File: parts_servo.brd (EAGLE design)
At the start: 27.1 x 50 mm, 43 parts, among them Q110 PMDPB28UN, Q120 PMDPB28UN, U1 MCP1703-3302, U100 RT9625A, U20 sn65hvd72, U50 nRF51822, X60 CX3225GB16000P0HPQCC

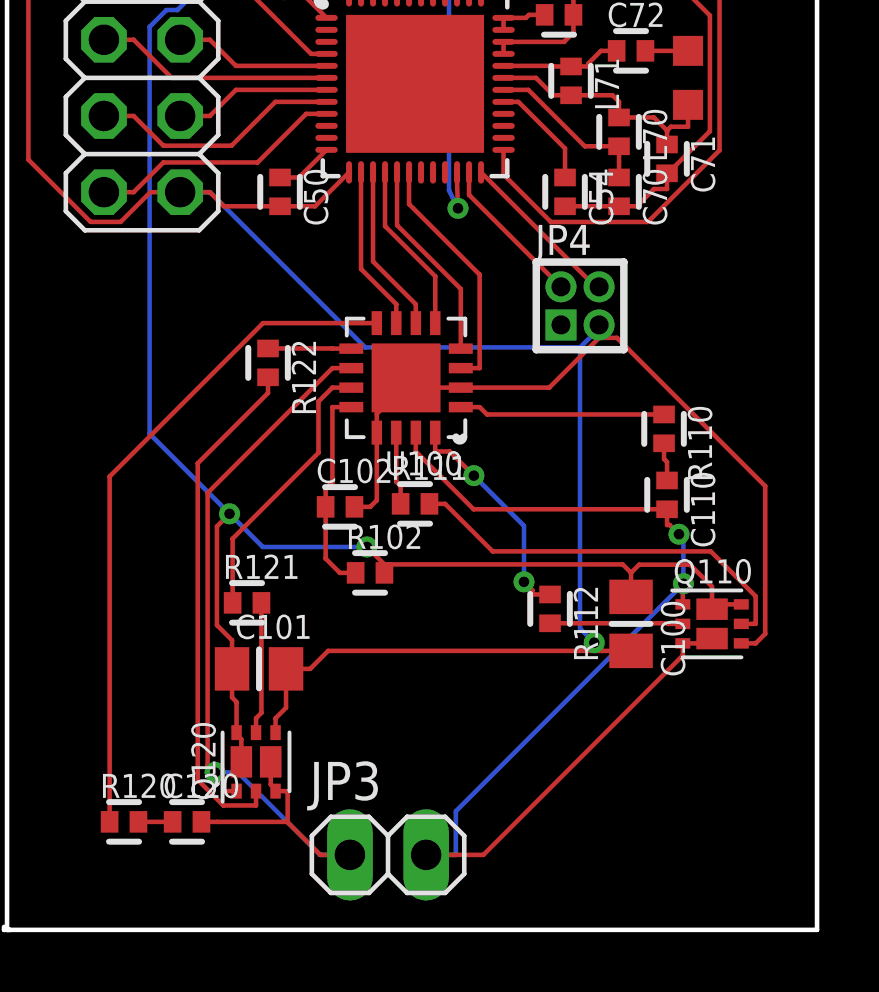
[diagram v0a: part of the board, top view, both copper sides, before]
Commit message: Fix DRC errors from via resize
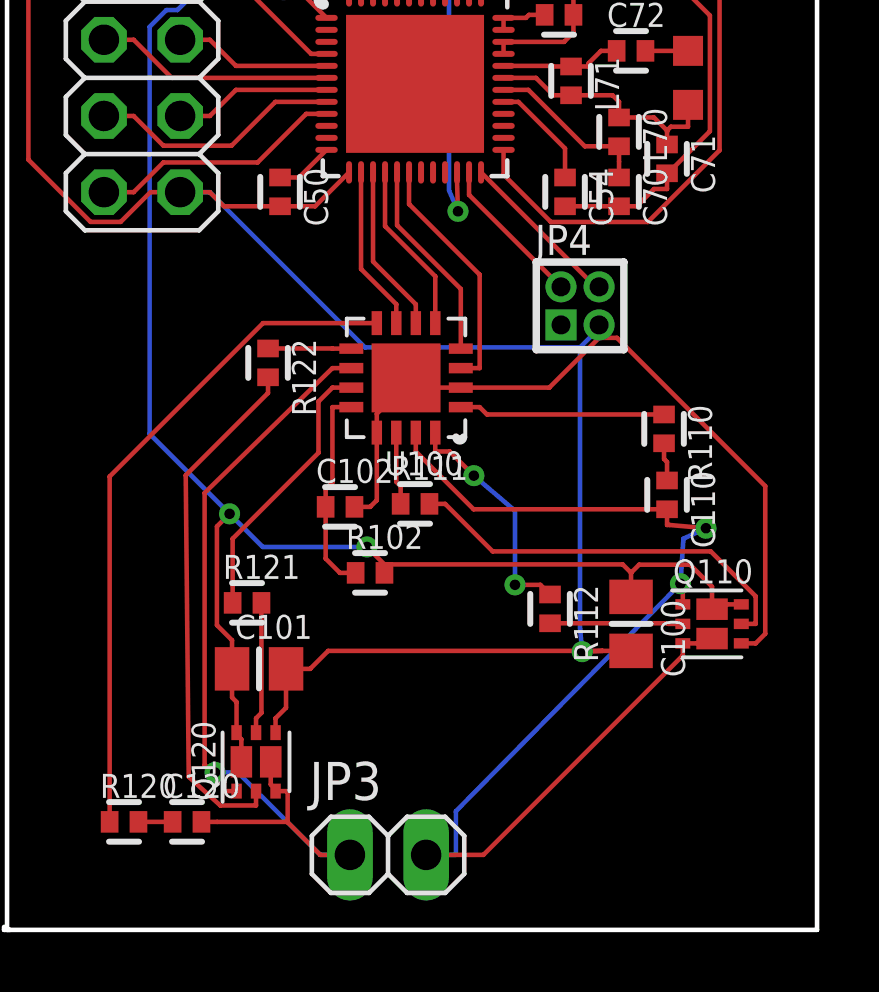
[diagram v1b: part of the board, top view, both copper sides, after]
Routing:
- net MOTOR2: track 39.2 -> 40.6 mm
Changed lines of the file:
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@@
 <contactref element="Q110" pad="4"/>
 <contactref element="Q120" pad="4"/>
-<wire x1="19.5733" y1="9.573" x2="19.8463" y2="9.3" width="0.1524" layer="1"/>
+<wire x1="19.1733" y1="9.273" x2="19.8463" y2="9.3" width="0.1524" layer="1"/>
 <wire x1="19.1" y1="19.4162" x2="19.1" y2="10.0463" width="0.1524" layer="16"/>
-<wire x1="19.1" y1="10.0463" x2="19.5733" y2="9.573" width="0.1524" layer="16"/>
+<wire x1="19.1" y1="10.0463" x2="19.1733" y2="9.273" width="0.1524" layer="16"/>
 <wire x1="19.735" y1="19.7344" x2="20.3311" y2="19.7344" width="0.1524" layer="1"/>
 <wire x1="20.3311" y1="19.7344" x2="25.2733" y2="14.7922" width="0.1524" layer="1"/>
@@
 <wire x1="6.7607" y1="24.59" x2="11.9345" y2="19.4162" width="0.1524" layer="16"/>
 <wire x1="11.9345" y1="19.4162" x2="19.1" y2="19.4162" width="0.1524" layer="16"/>
-<via x="19.5733" y="9.573" extent="1-16" drill="0.35" diameter="0.6858"/>
+<via x="19.1733" y="9.273" extent="1-16" drill="0.35" diameter="0.6858"/>
 <wire x1="19.8463" y1="9.3" x2="10.7037" y2="9.3" width="0.1524" layer="1"/>
 <wire x1="10.7037" y1="9.3" x2="10.1037" y2="8.7" width="0.1524" layer="1"/>
@@
 <contactref element="Q120" pad="P8"/>
 <contactref element="Q120" pad="1"/>
-<wire x1="10.8463" y1="18.725" x2="6.6856" y2="14.5643" width="0.1524" layer="1"/>
-<wire x1="6.6856" y1="14.5643" x2="6.6856" y2="5.4965" width="0.1524" layer="1"/>
-<wire x1="6.6856" y1="5.4965" x2="6.9337" y2="5.2484" width="0.1524" layer="1"/>
+<wire x1="10.8463" y1="18.725" x2="6.5856" y2="14.5643" width="0.1524" layer="1"/>
+<wire x1="6.5856" y1="14.5643" x2="6.5856" y2="5.4965" width="0.1524" layer="1"/>
+<wire x1="6.5856" y1="5.4965" x2="6.9337" y2="5.2484" width="0.1524" layer="1"/>
 <wire x1="7.2463" y1="4.625" x2="7.2463" y2="4.9358" width="0.1524" layer="1"/>
 <wire x1="7.2463" y1="4.9358" x2="6.9337" y2="5.2484" width="0.1524" layer="1"/>
@@
 <contactref element="R122" pad="2"/>
 <contactref element="Q120" pad="2"/>
-<wire x1="8.3" y1="4.1463" x2="7.2101" y2="4.1463" width="0.1524" layer="1"/>
-<wire x1="7.2101" y1="4.1463" x2="6.356" y2="5.0004" width="0.1524" layer="1"/>
-<wire x1="6.356" y1="5.0004" x2="6.356" y2="15.5523" width="0.1524" layer="1"/>
-<wire x1="6.356" y1="15.5523" x2="8.7" y2="17.8963" width="0.1524" layer="1"/>
+<wire x1="8.3" y1="4.1463" x2="7.1101" y2="4.1463" width="0.1524" layer="1"/>
+<wire x1="7.1101" y1="4.1463" x2="6.056" y2="5.1004" width="0.1524" layer="1"/>
+<wire x1="6.056" y1="5.1004" x2="5.956" y2="15.1523" width="0.1524" layer="1"/>
+<wire x1="5.956" y1="15.1523" x2="8.7" y2="17.8963" width="0.1524" layer="1"/>
 <wire x1="8.3" y1="4.625" x2="8.3" y2="4.1463" width="0.1524" layer="1"/>
 <wire x1="8.7" y1="18.42" x2="8.7" y2="17.8963" width="0.1524" layer="1"/>
@@
 <wire x1="13.97" y1="2.5" x2="15.8787" y2="2.5" width="0.1524" layer="1"/>
 <wire x1="15.8787" y1="2.5" x2="22.525" y2="9.1463" width="0.1524" layer="1"/>
-<wire x1="22.5461" y1="11.5393" x2="22.525" y2="11.5182" width="0.1524" layer="1"/>
+<wire x1="22.4461" y1="11.5393" x2="22.525" y2="11.5182" width="0.1524" layer="1"/>
 <wire x1="22.525" y1="11.5182" x2="22.525" y2="10.85" width="0.1524" layer="1"/>
 <wire x1="22" y1="14.02" x2="22" y2="13.4963" width="0.1524" layer="1"/>
 <wire x1="22" y1="13.4963" x2="22.0895" y2="13.4963" width="0.1524" layer="1"/>
-<wire x1="22.0895" y1="13.4963" x2="22.3977" y2="13.1881" width="0.1524" layer="1"/>
-<wire x1="22.3977" y1="13.1881" x2="22.5461" y2="13.0397" width="0.1524" layer="16"/>
-<wire x1="22.5461" y1="13.0397" x2="22.5461" y2="11.5393" width="0.1524" layer="16"/>
-<via x="22.3977" y="13.1881" extent="1-16" drill="0.35" diameter="0.6858"/>
+<wire x1="22.0895" y1="13.4963" x2="23.2977" y2="13.3881" width="0.1524" layer="1"/>
+<wire x1="23.2977" y1="13.3881" x2="22.5461" y2="13.0397" width="0.1524" layer="16"/>
+<wire x1="22.5461" y1="13.0397" x2="22.4461" y2="11.5393" width="0.1524" layer="16"/>
+<via x="23.2977" y="13.3881" extent="1-16" drill="0.35" diameter="0.6858"/>
 <wire x1="13.625" y1="15.9463" x2="15.5513" y2="14.02" width="0.1524" layer="1"/>
 <wire x1="15.5513" y1="14.02" x2="22" y2="14.02" width="0.1524" layer="1"/>
 <wire x1="13.97" y1="2.5" x2="14.9607" y2="2.5" width="0.1524" layer="16"/>
 <wire x1="14.9607" y1="2.5" x2="14.9607" y2="3.9539" width="0.1524" layer="16"/>
-<wire x1="14.9607" y1="3.9539" x2="22.5461" y2="11.5393" width="0.1524" layer="16"/>
-<via x="22.5461" y="11.5393" extent="1-16" drill="0.35" diameter="0.6858"/>
+<wire x1="14.9607" y1="3.9539" x2="22.4461" y2="11.5393" width="0.1524" layer="16"/>
+<via x="22.4461" y="11.5393" extent="1-16" drill="0.35" diameter="0.6858"/>
 <wire x1="13.625" y1="16.575" x2="13.625" y2="15.9463" width="0.1524" layer="1"/>
 <wire x1="22.525" y1="9.55" x2="22.569" y2="9.55" width="0.1524" layer="1"/>
@@
 <contactref element="R112" pad="1"/>
 <contactref element="U100" pad="16"/>
-<wire x1="17.5113" y1="11.18" x2="17.5113" y2="11.3216" width="0.1524" layer="1"/>
-<wire x1="17.5113" y1="11.3216" x2="17.2315" y2="11.6014" width="0.1524" layer="1"/>
-<wire x1="15.5609" y1="15.1405" x2="17.2315" y2="13.4699" width="0.1524" layer="16"/>
-<wire x1="17.2315" y1="13.4699" x2="17.2315" y2="11.6014" width="0.1524" layer="16"/>
-<wire x1="18.1" y1="11.18" x2="17.5113" y2="11.18" width="0.1524" layer="1"/>
+<wire x1="15.5609" y1="15.1405" x2="16.9315" y2="13.9699" width="0.1524" layer="16"/>
+<wire x1="16.9315" y1="13.9699" x2="16.9315" y2="11.5014" width="0.1524" layer="16"/>
 <wire x1="14.275" y1="16.575" x2="14.275" y2="15.9463" width="0.1524" layer="1"/>
 <wire x1="15.5609" y1="15.1405" x2="14.7551" y2="15.9463" width="0.1524" layer="1"/>
 <wire x1="14.7551" y1="15.9463" x2="14.275" y2="15.9463" width="0.1524" layer="1"/>
 <via x="15.5609" y="15.1405" extent="1-16" drill="0.35" diameter="0.6858"/>
-<via x="17.2315" y="11.6014" extent="1-16" drill="0.35" diameter="0.6858"/>
+<via x="16.9315" y="11.5014" extent="1-16" drill="0.35" diameter="0.6858"/>
+<wire x1="16.9315" y1="11.5014" x2="17.7786" y2="11.5014" width="0.1524" layer="1"/>
+<wire x1="17.7786" y1="11.5014" x2="18.1" y2="11.18" width="0.1524" layer="1"/>
 </signal>
 <signal name="BOOT2">
@@
 <contactref element="U50" pad="22"/>
 <wire x1="15" y1="25.25" x2="15" y2="24.9197" width="0.1524" layer="1"/>
-<wire x1="15" y1="24.9197" x2="15.0317" y2="24.0514" width="0.1524" layer="1"/>
+<wire x1="15" y1="24.9197" x2="15.0317" y2="23.9514" width="0.1524" layer="1"/>
 <wire x1="9.1786" y1="41.3827" x2="14.7316" y2="35.8297" width="0.1524" layer="16"/>
 <wire x1="14.7316" y1="35.8297" x2="14.7316" y2="24.6514" width="0.1524" layer="16"/>
-<wire x1="14.7316" y1="24.6514" x2="15.0317" y2="24.0514" width="0.1524" layer="16"/>
+<wire x1="14.7316" y1="24.6514" x2="15.0317" y2="23.9514" width="0.1524" layer="16"/>
 <wire x1="8.22" y1="42.9" x2="8.22" y2="42.3113" width="0.1524" layer="1"/>
 <wire x1="9.1786" y1="41.3827" x2="8.25" y2="42.3113" width="0.1524" layer="1"/>
 <wire x1="8.25" y1="42.3113" x2="8.22" y2="42.3113" width="0.1524" layer="1"/>
 <via x="9.1786" y="41.3827" extent="1-16" drill="0.35" diameter="0.6858"/>
-<via x="15.0317" y="24.0514" extent="1-16" drill="0.35" diameter="0.6858"/>
+<via x="15.0317" y="23.9514" extent="1-16" drill="0.35" diameter="0.6858"/>
 </signal>
 <signal name="DIFFERENTIAL_OUTPUT">

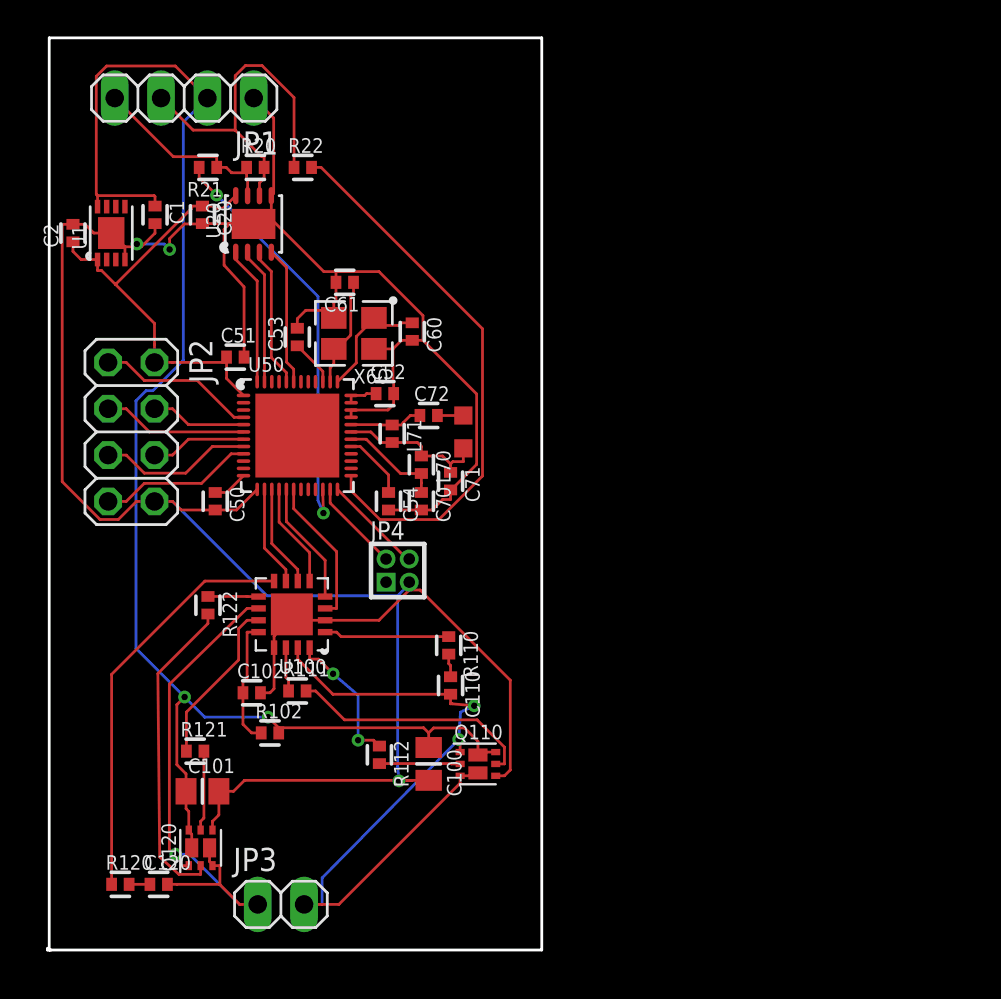
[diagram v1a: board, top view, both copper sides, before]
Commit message: Fatten some traces, fix DRC and routing
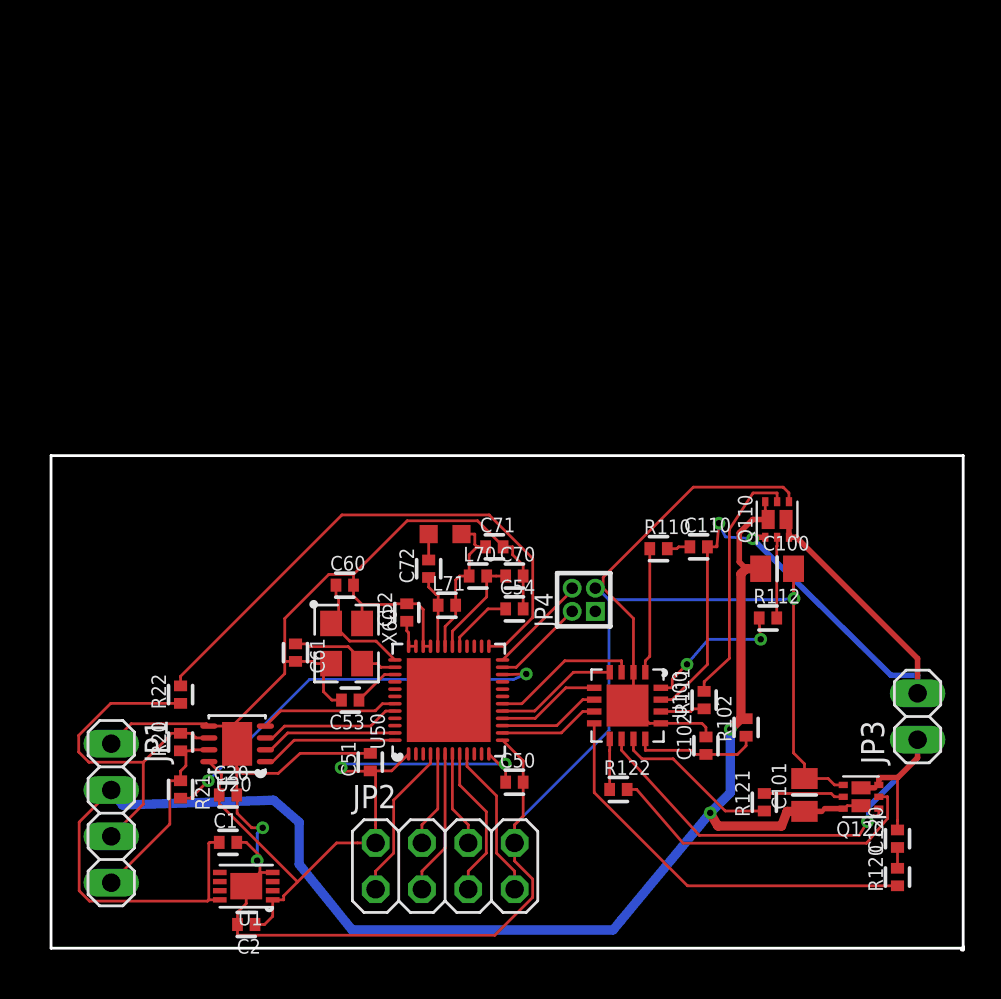
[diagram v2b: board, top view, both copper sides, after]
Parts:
- moved R120 42.6 mm to (46.5, 4.00), turned to 90 degrees
- moved C120 40.6 mm to (46.5, 6.10), turned to 90 degrees
- moved JP1 39.4 mm to (3.40, 7.50), turned to 270 degrees
- moved C2 39.1 mm to (10.8, 1.40), turned to 180 degrees
- moved U1 36.6 mm to (10.8, 3.50), turned to 180 degrees
- moved JP3 36.4 mm to (47.6, 12.8), turned to 90 degrees
- moved Q120 36.3 mm to (44.5, 8.40), turned to 180 degrees
- moved C1 34.6 mm to (9.80, 5.90), turned to 0 degrees
- moved R21 34.1 mm to (7.20, 8.80), turned to 270 degrees
- moved C101 33.0 mm to (41.4, 8.50), turned to 90 degrees
- moved C20 31.8 mm to (9.80, 8.50), turned to 0 degrees
- moved R20 31.8 mm to (7.20, 11.4), turned to 90 degrees
- moved R121 31.3 mm to (39.2, 8.10), turned to 90 degrees
- moved R22 29.7 mm to (7.20, 14.0), turned to 90 degrees
- moved JP2 29.4 mm to (21.7, 4.60), turned to 0 degrees
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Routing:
- net 3.3V: track 26.4 -> 37.6 mm, vias 0 -> 2
- net POWER_IN: track 82.6 -> 88.3 mm
- net MOTOR1: track 30.8 -> 31.3 mm
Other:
- board size 27.1 x 50 mm -> 50 x 27.1 mm

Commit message: Move programming header to edge of board
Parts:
- moved JP4 5.90 mm to (29.4, 25.1)
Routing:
- net GND: track 165.6 -> 175.8 mm
- net SWDCLK: track 5.52 -> 11.6 mm
- net SWDIO: track 5.08 -> 10.9 mm
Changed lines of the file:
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@@
 </element>
 <element name="U20" library="parts_servo" package="DFN-8(3X3)+EP" value="sn65hvd72" x="10.3" y="11.3" rot="R180"/>
-<element name="JP4" library="parts_servo" package="PINHEADER-2X2-0.05_IN" value="SWD" x="29.3" y="19.2" rot="R90"/>
+<element name="JP4" library="parts_servo" package="PINHEADER-2X2-0.05_IN" value="SWD" x="29.4" y="25.1" rot="R90"/>
 <element name="Q110" library="parts_servo" package="DFN-6(2X2)+2EP(TRANSISTOR)" value="PMDPB28UN" x="39.9" y="23.6" rot="R90"/>
 <element name="JP2" library="pinhead" package="2X04" value="Sensor" x="21.7" y="4.6"/>
@@
 <wire x1="30.6838" y1="19.2" x2="40.0537" y2="19.2" width="0.1524" layer="16"/>
 <wire x1="40.0537" y1="19.2" x2="40.827" y2="19.2733" width="0.1524" layer="16"/>
-<wire x1="30.3656" y1="19.835" x2="30.3656" y2="20.4311" width="0.1524" layer="1"/>
-<wire x1="30.3656" y1="20.4311" x2="35.3078" y2="25.3733" width="0.1524" layer="1"/>
-<wire x1="35.3078" y1="25.3733" x2="40.2304" y2="25.3733" width="0.1524" layer="1"/>
-<wire x1="40.2304" y1="25.3733" x2="40.55" y2="25.0537" width="0.1524" layer="1"/>
-<wire x1="32.025" y1="15.225" x2="32.025" y2="18.1756" width="0.1524" layer="1"/>
-<wire x1="32.025" y1="18.1756" x2="30.3656" y2="19.835" width="0.1524" layer="1"/>
-<wire x1="29.935" y1="19.835" x2="30.3656" y2="19.835" width="0.1524" layer="1"/>
-<wire x1="40.55" y1="24.575" x2="40.55" y2="25.0537" width="0.1524" layer="1"/>
 <wire x1="20.9" y1="16.65" x2="20.9" y2="16.55" width="0.1524" layer="1"/>
 <wire x1="24.7741" y1="11.5" x2="24.85" y2="11.5" width="0.1524" layer="1"/>
 <wire x1="12.5569" y1="9.6847" x2="13.7522" y2="10.78" width="0.1524" layer="1"/>
 <wire x1="13.7522" y1="10.78" x2="17.6" y2="10.78" width="0.1524" layer="1"/>
-<wire x1="30.6838" y1="19.2" x2="30.0488" y2="19.835" width="0.1524" layer="16"/>
-<wire x1="30.0488" y1="19.835" x2="29.935" y2="19.835" width="0.1524" layer="16"/>
+<wire x1="30.6838" y1="19.2" x2="31.5488" y2="19.935" width="0.1524" layer="16"/>
+<wire x1="31.5488" y1="19.935" x2="31.6" y2="24.4" width="0.1524" layer="16"/>
+<wire x1="31.6" y1="24.4" x2="31.6" y2="24.835" width="0.1524" layer="16"/>
+<wire x1="31.6" y1="24.835" x2="30.035" y2="25.735" width="0.1524" layer="16"/>
 <wire x1="25.51" y1="6.8607" x2="30.6838" y2="12.0345" width="0.1524" layer="16"/>
 <wire x1="30.6838" y1="12.0345" x2="30.6838" y2="19.2" width="0.1524" layer="16"/>
@@
 <via x="11.7" y="6.7" extent="1-16" drill="0.35" diameter="0.6358"/>
 <via x="11.4" y="4.9" extent="1-16" drill="0.35" diameter="0.6358"/>
+<wire x1="32.025" y1="15.225" x2="32.025" y2="18.1756" width="0.1524" layer="1"/>
+<wire x1="40.55" y1="24.575" x2="40.525" y2="24.575" width="0.1524" layer="1"/>
+<wire x1="40.525" y1="24.575" x2="40.5" y2="24.6" width="0.1524" layer="1"/>
+<wire x1="40.5" y1="24.6" x2="40.5" y2="25.1" width="0.1524" layer="1"/>
+<wire x1="40.5" y1="25.1" x2="39.8" y2="25.8" width="0.1524" layer="1"/>
+<wire x1="39.8" y1="25.8" x2="30.6" y2="25.8" width="0.1524" layer="1"/>
+<wire x1="30.6" y1="25.8" x2="30.1" y2="25.8" width="0.1524" layer="1"/>
+<wire x1="30.1" y1="25.8" x2="30.035" y2="25.735" width="0.1524" layer="1"/>
+<wire x1="32.025" y1="18.1756" x2="32.025" y2="24.375" width="0.1524" layer="1"/>
+<wire x1="32.025" y1="24.375" x2="30.6" y2="25.8" width="0.1524" layer="1"/>
 </signal>
 <signal name="HSCLK_IN">
@@
 <contactref element="JP4" pad="2"/>
 <contactref element="U50" pad="23"/>
-<wire x1="24.85" y1="15.5" x2="25.6" y2="15.5" width="0.1524" layer="1"/>
-<wire x1="25.6" y1="15.5" x2="28.665" y2="18.565" width="0.1524" layer="1"/>
+<wire x1="24.85" y1="15.5" x2="25.3" y2="15.5" width="0.1524" layer="1"/>
+<wire x1="25.3" y1="15.5" x2="27.6" y2="17.8" width="0.1524" layer="1"/>
+<wire x1="27.6" y1="17.8" x2="27.6" y2="23.3" width="0.1524" layer="1"/>
+<wire x1="27.6" y1="23.3" x2="28.765" y2="24.465" width="0.1524" layer="1"/>
 </signal>
 <signal name="SWDCLK">
 <contactref element="JP4" pad="4"/>
 <contactref element="U50" pad="24"/>
-<wire x1="24.85" y1="15.9" x2="28.665" y2="19.715" width="0.1524" layer="1"/>
-<wire x1="28.665" y1="19.715" x2="28.665" y2="19.835" width="0.1524" layer="1"/>
+<wire x1="24.85" y1="15.9" x2="25.1" y2="15.9" width="0.1524" layer="1"/>
+<wire x1="25.1" y1="15.9" x2="27.1" y2="17.9" width="0.1524" layer="1"/>
+<wire x1="27.1" y1="17.9" x2="27.1" y2="24.07" width="0.1524" layer="1"/>
+<wire x1="27.1" y1="24.07" x2="28.765" y2="25.735" width="0.1524" layer="1"/>
 </signal>
 <signal name="POWER_IN">
